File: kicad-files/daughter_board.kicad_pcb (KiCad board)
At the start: 2 copper layers, 22 x 25 mm, 19 parts, among them J1 TYPE-C-31-M12_13, T1 53261-0471, U1 TPD4E05U06DQAR, U2 MCP1700T-3302E/TT

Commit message: Finished adding parts to the daughter board
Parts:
- F1: value nSMD100-16V -> SMD0805-050-16V
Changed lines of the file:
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@@
         (effects (font (size 0.9 0.9) (thickness 0.15)))
     )
-    (fp_text value "nSMD100-16V" (at 0 1.82) (layer "F.Fab")
+    (fp_text value "SMD0805-050-16V" (at 0 1.82) (layer "F.Fab")
         (effects (font (size 1 1) (thickness 0.15)))
     )

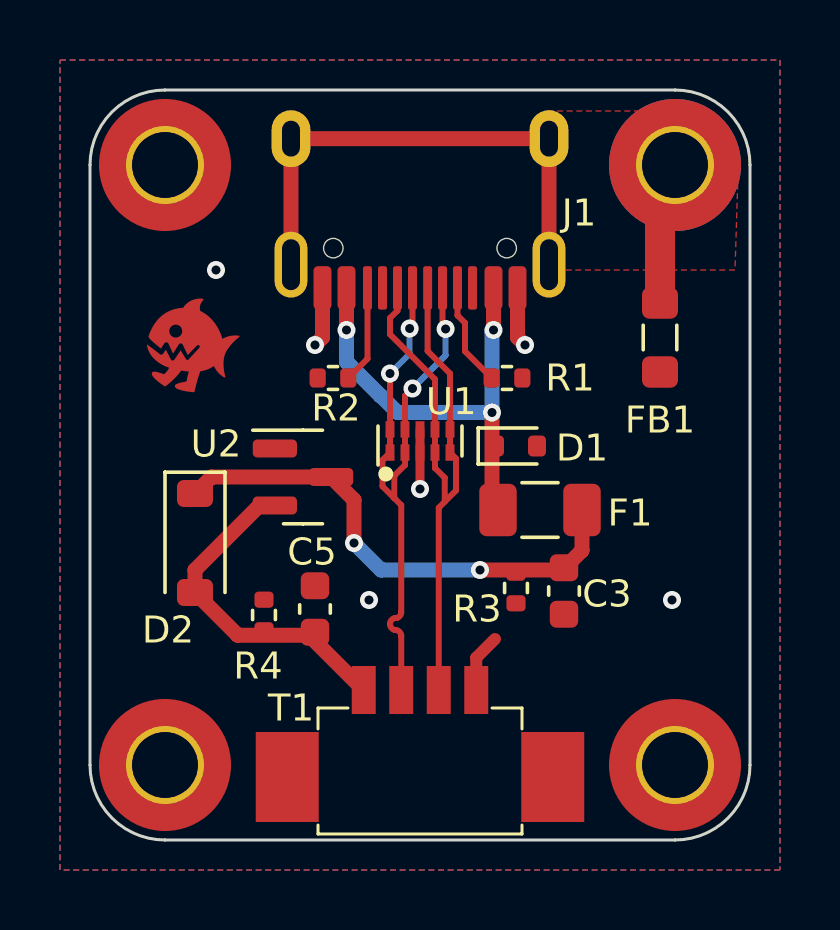
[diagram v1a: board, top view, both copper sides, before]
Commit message: Added header for 5V on daughter board and updated BOM a little
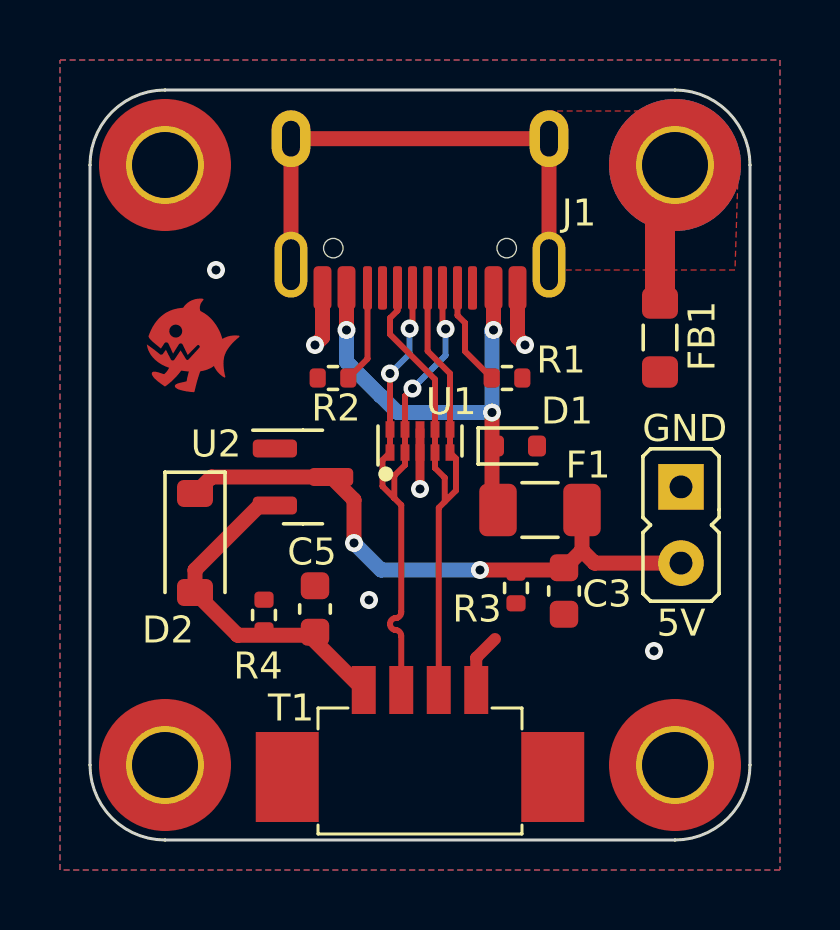
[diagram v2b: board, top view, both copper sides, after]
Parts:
- added J2: Conn_01x02, acheron_Connectors:PinHeader_1x2_P2.54mm_Vertical, F.Cu at (108.7, 92.5)
- C3, C5: value 1u -> 1uF
- D2: value 1N5819WS -> B5819W-SL
- J1: value TYPE-C-31-M12_13 -> TYPE-C-31-M-12
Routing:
- net 5V: track 16.9 -> 20.3 mm
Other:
- board text added: "5V"
- board text added: "GND"

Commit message: Updated small things on daughter board bom
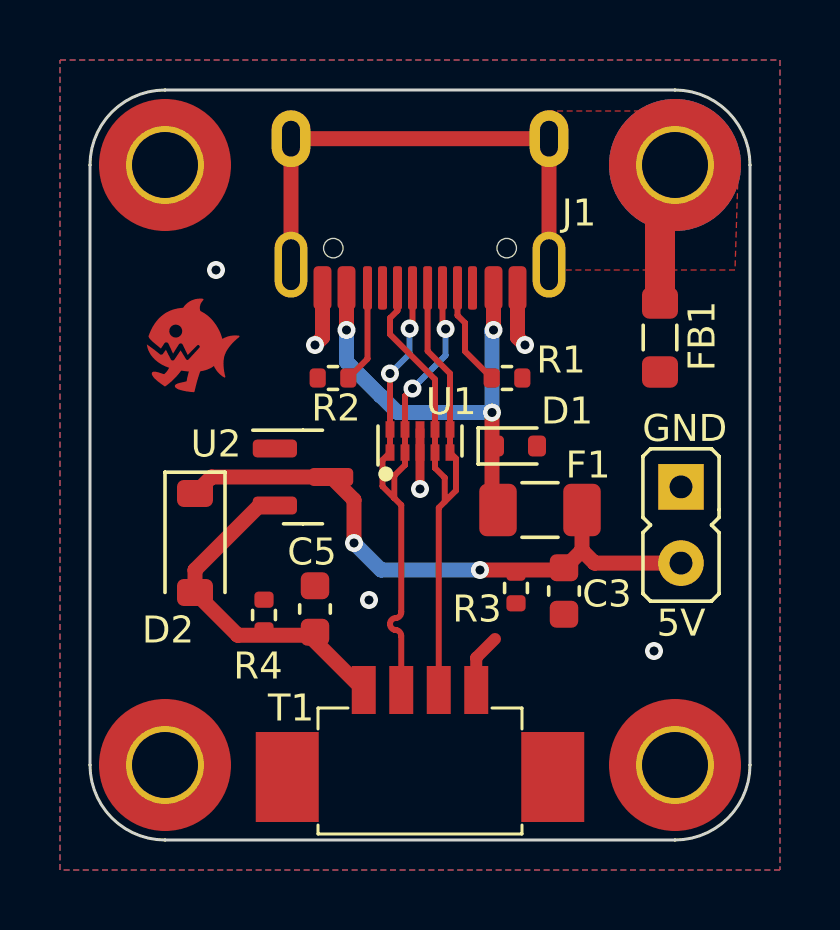
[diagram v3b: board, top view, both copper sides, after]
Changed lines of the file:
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@@
     )
     (pad_to_mask_clearance 0)
-    (aux_axis_origin 91.5 80.517767)
+    (aux_axis_origin 100 90.5)
     (pcbplotparams
       (layerselection 0x00010fc_ffffffff)
@@
       (viasonmask false)
       (mode 1)
-      (useauxorigin false)
+      (useauxorigin true)
       (hpglpennumber 1)
       (hpglpenspeed 20)
@@
       (outputformat 1)
       (mirror false)
-      (drillshape 1)
+      (drillshape 0)
       (scaleselection 1)
-      (outputdirectory "")
+      (outputdirectory "../plots/")
     )
   )
@@
     (fp_line (start 1 0.45) (end -1 0.45)
       (stroke (width 0.1) (type solid)) (layer "F.Fab"))
-    (pad "1" smd roundrect (at -1.15 0 270) (size 1.05 1.2) (layers "F.Cu" "F.Paste" "F.Mask") (roundrect_rratio 0.238095)
+    (pad "1" smd roundrect (at -1.15 0 270) (size 1.05 1.2) (layers "F.Cu" "F.Paste" "F.Mask") (roundrect_rratio 0.2380952381)
       (net 3 "GNDPWR") (pintype "passive"))
-    (pad "2" smd roundrect (at 1.15 0 270) (size 1.05 1.2) (layers "F.Cu" "F.Paste" "F.Mask") (roundrect_rratio 0.238095)
+    (pad "2" smd roundrect (at 1.15 0 270) (size 1.05 1.2) (layers "F.Cu" "F.Paste" "F.Mask") (roundrect_rratio 0.2380952381)
       (net 2 "GND") (pintype "passive"))
     (model "${KICAD6_3DMODEL_DIR}/Inductor_SMD.3dshapes/L_0805_2012Metric.wrl"
@@
     )
   )
+  (gr_line (start 100 78) (end 100 103)
+    (stroke (width 0.15) (type default)) (layer "Dwgs.User"))
   (gr_line (start 91.5 78) (end 108.5 78)
     (stroke (width 0.1) (type default)) (layer "Edge.Cuts"))
@@
     (effects (font (size 0.9 0.9) (thickness 0.15)) (justify left bottom))
   )
+  (dimension (type aligned) (layer "Dwgs.User")
+    (pts (xy 100 78) (xy 100 103))
+    (height -17.8)
+    (gr_text "25.0000 mm" (at 116.65 90.5 90) (layer "Dwgs.User")
+      (effects (font (size 1 1) (thickness 0.15)))
+    )
+    (format (prefix "") (suffix "") (units 3) (units_format 1) (precision 4))
+    (style (thickness 0.15) (arrow_length 1.27) (text_position_mode 0) (extension_height 0.58642) (extension_offset 0.5) keep_text_aligned)
+  )
+  (dimension (type aligned) (layer "Dwgs.User")
+    (pts (xy 100 78) (xy 100 90.5))
+    (height -22.4)
+    (gr_text "12.5000 mm" (at 121.25 84.25 90) (layer "Dwgs.User")
+      (effects (font (size 1 1) (thickness 0.15)))
+    )
+    (format (prefix "") (suffix "") (units 3) (units_format 1) (precision 4))
+    (style (thickness 0.15) (arrow_length 1.27) (text_position_mode 0) (extension_height 0.58642) (extension_offset 0.5) keep_text_aligned)
+  )
   (segment (start 104.75 94) (end 105.4 93.35) (width 0.5) (layer "F.Cu") (net 1))
   (segment (start 97.8 91.6625) (end 97.0375 90.9) (width 0.5) (layer "F.Cu") (net 1))
@@
   (segment (start 99 90.085) (end 98.75 90.335) (width 0.2) (layer "F.Cu") (net 11))
   (segment (start 99 90.085) (end 99 88.4) (width 0.2) (layer "F.Cu") (net 11))
-  (segment (start 99.175 95.6) (end 99.214591 95.599039) (width 0.2) (layer "F.Cu") (net 11))
-  (segment (start 99.21363 95.6) (end 99.214591 95.599039) (width 0.2) (layer "F.Cu") (net 11))
   (segment (start 99.75 84.5975) (end 99.75 85.8545) (width 0.2) (layer "F.Cu") (net 11))
   (segment (start 99.175 96) (end 99.2 96) (width 0.2) (layer "F.Cu") (net 11))
   (segment (start 99 88.4) (end 99 87.45) (width 0.2) (layer "F.Cu") (net 11))
   (segment (start 99.75 85.8545) (end 99.6545 85.95) (width 0.2) (layer "F.Cu") (net 11))
-  (segment (start 99.2 95.6) (end 99.21363 95.6) (width 0.2) (layer "F.Cu") (net 11))
   (segment (start 98.75 91.21) (end 99.145 91.605) (width 0.2) (layer "F.Cu") (net 11))
   (segment (start 99.5 90.5) (end 99.5 90.085) (width 0.2) (layer "F.Cu") (net 11))
